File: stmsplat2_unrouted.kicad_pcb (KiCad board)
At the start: 2 copper layers, 100 x 100 mm, 113 parts, among them J1 C11_2X36, J10 Conn_01x03_Male, J11 Conn_01x02_Male, J12 Conn_01x04_Male, J13 Conn_01x04_Male, J14 Conn_01x02, J15 Conn_01x02, J16 Screw_Terminal_01x03, J17 Screw_Terminal_01x02, J2 C12_2X36, J3 Conn_01x04_Male, J4 Conn_01x04_Male, J5 Conn_Coaxial, J6 Conn_01x04_Male, J7 Conn_01x04_Male, J8 Conn_01x04_Male, J9 Conn_01x03_Male, Q1 BSS138LT1G, U1 ublox_chinese_PCB_module, U10 XCVR_E30-400M20S (Si4463), U11 3115_module, U2 ESP-C3-13U, U3 SST25VF032B, U4 48L512-48LM01, U5 Opamp_Quad_MCP6024, U6 E180-ZG120A, U7 AZ1084C, U8 MCP6S93-X_UN, U9 DS2485

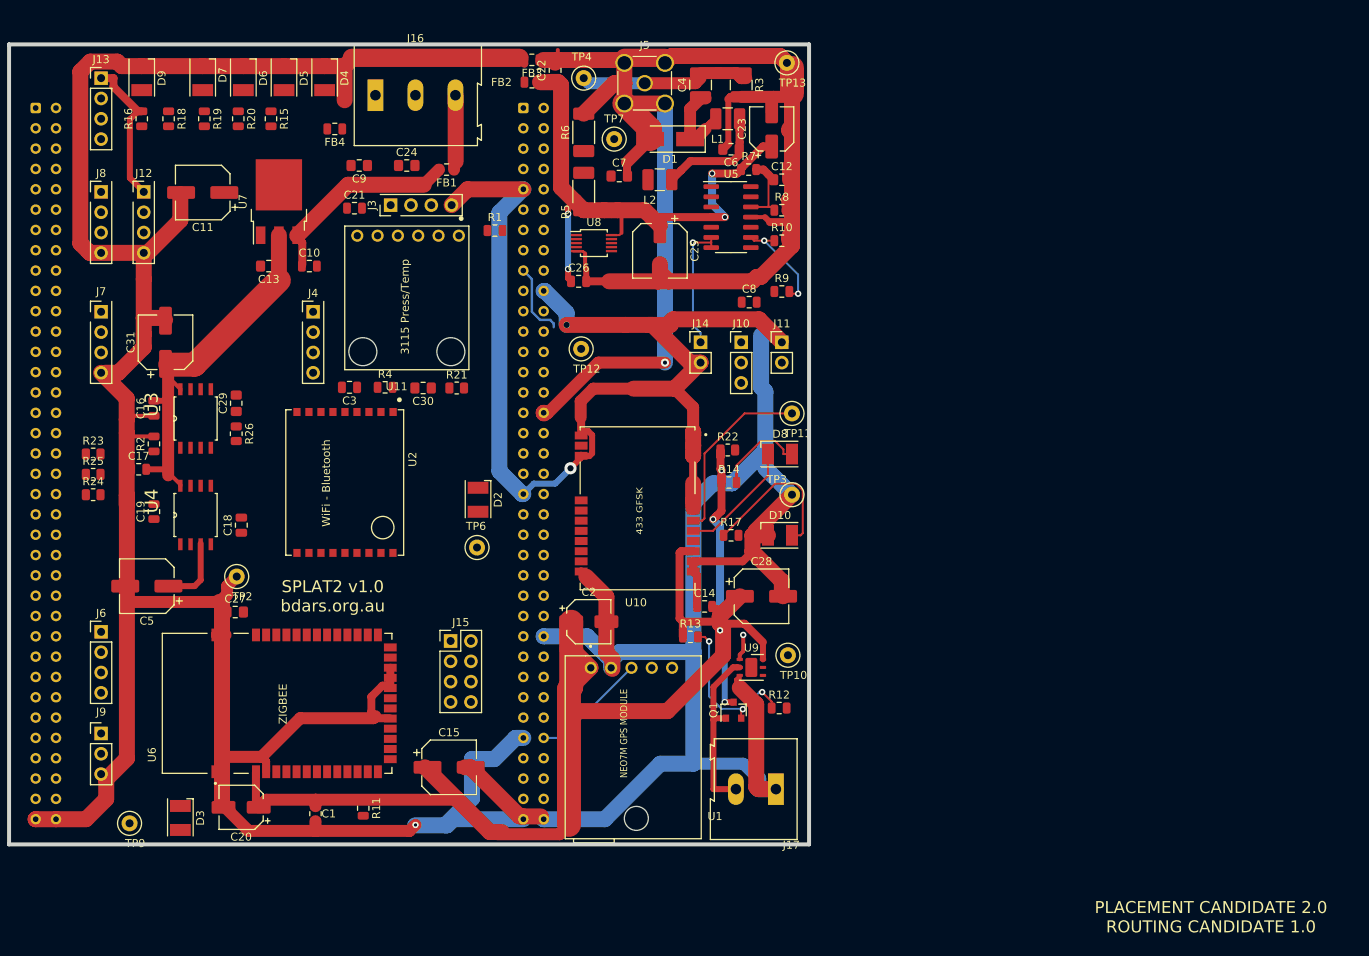
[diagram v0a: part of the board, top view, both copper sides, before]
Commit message: better placement, more handrouting, re-done power area etc
A few more passive comps added including dil switch
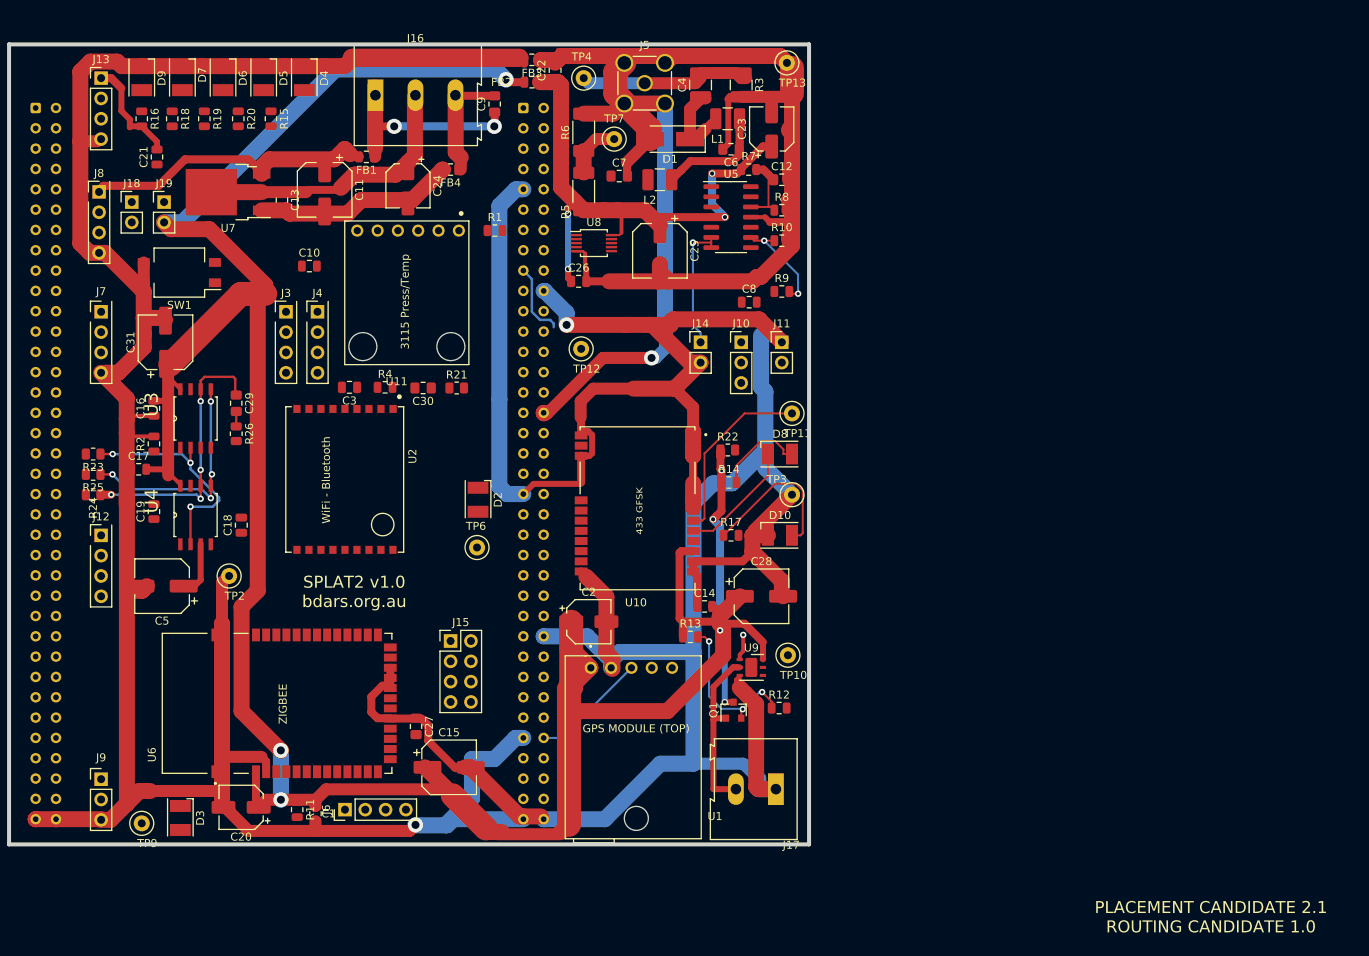
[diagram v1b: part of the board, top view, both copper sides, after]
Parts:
- added J18: Conn_01x02_Male, Connector_PinHeader_2.54mm:PinHeader_1x02_P2.54mm_Vertical, F.Cu at (67.3, 85.3)
- added J19: Conn_01x02_Male, Connector_PinHeader_2.54mm:PinHeader_1x02_P2.54mm_Vertical, F.Cu at (71.4, 85.3)
- added SW1: SW_DIP_x02, Button_Switch_SMD:SW_DIP_SPSTx02_Slide_Omron_A6S-210x_W8.9mm_P2.54mm, F.Cu at (73.3, 94.2)
- C24: value 0.1uF -> 10uF; footprint Capacitor_SMD:C_0805_2012Metric_Pad1.15x1.40mm_HandSolder -> Capacitor_SMD:CP_Elec_5x5.4
- moved J12 43.3 mm to (63.5, 127.0)
- moved J6 37.7 mm to (94.0, 161.3), turned to 90 degrees
- moved C27 26.7 mm to (102.9, 150.9), turned to 270 degrees
- moved C21 25.5 mm to (70.5, 79.7), turned to 90 degrees
- moved J3 18.7 mm to (86.6, 99.1), turned to 0 degrees
- moved C9 18.6 mm to (112.7, 73.1), turned to 90 degrees
- moved FB4 15.3 mm to (107.2, 81.3)
- moved C11 15.2 mm to (91.4, 83.8), turned to 270 degrees
- moved FB1 10.1 mm to (96.7, 79.7)
- moved C13 8.42 mm to (86.1, 85.1), turned to 270 degrees
- moved R11 8.26 mm to (88.0, 161.3)
- moved U7 6.46 mm to (79.4, 84.1), turned to 180 degrees
- moved J9 5.72 mm to (63.5, 157.5)
- moved C24 2.54 mm to (101.9, 83.3), turned to 270 degrees
- moved D5 2.54 mm to (83.8, 69.8)
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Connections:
- C13 pad 1: VDD -> Net-(C13-Pad1)
- C24 pad 1: VDD -> Net-(C13-Pad1)
- C24 pad 2: /RAWGND -> GND
- J1 pad 14: /NRST -> NRST
- J1 pad 4: /PD2 -> PD2
- J1 pad 45: /PD7 -> PD7
- J16 pad 1: /RAWGND -> /RAW5V
- J16 pad 2: VDD -> Net-(C13-Pad1)
- J16 pad 3: /RAW5V -> /RAWGND
- U7 pad 2: VDD -> Net-(C13-Pad1)
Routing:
- net VDD: track 248.0 -> 371.4 mm, vias 4 -> 7
- net /SPI2_SCKT: track 0.00 -> 35.1 mm, vias 0 -> 4
- net Net-(C13-Pad1): track 0.00 -> 34.6 mm
- net /SPI2_MOSIT: track 0.00 -> 28.9 mm, vias 0 -> 4
- net /SPI2_MISOT: track 0.00 -> 28.4 mm, vias 0 -> 3
- net /RAW5V: track 9.36 -> 25.3 mm, vias 0 -> 2
- net /RAWGND: track 0.00 -> 14.3 mm
- net +5V: track 25.1 -> 37.8 mm
- net GND: track 684.5 -> 694.1 mm, vias 3 -> 2
- net Net-(C7-Pad1): track 0.00 -> 7.09 mm
- net Net-(C5-Pad1): track 8.92 -> 6.92 mm
- net Net-(C29-Pad2): track 0.00 -> 1.85 mm
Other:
- board text added: "PLACEMENT CANDIDATE 2.1 ROUTING CANDIDATE 1.0"
- board text removed: "PLACEMENT CANDIDATE 2.0 ROUTING CANDIDATE 1.0"

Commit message: Splat2 Revision A.  Work-in-progress
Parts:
- removed REF**: ST_Morpho_Connector_144_STLink_MountingHoles, Module:ST_Morpho_Connector_144_STLink_MountingHoles
- D10, D2, D3, D4, D5, D6, D7, D8, D9: footprint LED_SMD:LED_PLCC-2 -> splat2footprints:LED_PLCC-2
- J1, J2: footprint Connector_Samtec_HLE_THT:Samtec_HLE-136-02-xx-DV-TE_2x36_P2.54mm_Horizontal -> Connector_PinSocket_2.54mm:PinSocket_2x36_P2.54mm_Vertical
- R5, R6: footprint Resistor_SMD:R_2010_5025Metric_Pad1.52x2.65mm_HandSolder -> Resistor_SMD:R_0805_2012Metric
- R7, R8: value 4K7 -> 1K
- moved R1 2.90 mm to (111.9, 86.1)
- moved TP10 2.07 mm to (149.8, 140.0)
- moved C2 0.93 mm to (125.3, 138.2)
- moved C11 0.51 mm to (90.9, 83.8)
- turned J1 to 180 degrees
- turned J2 to 180 degrees
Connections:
- net Net-(C13-Pad1) renamed /OUR3V3
- C1 pad 1: VDD -> +3V3
- C11 pad 1: +5V -> 5VEXT
- C14 pad 2: VDD -> +3V3
- C15 pad 1: VDD -> +3V3
- C16 pad 2: VDD -> +3V3
- C17 pad 2: VDD -> +3V3
- C18 pad 1: VDD -> +3V3
- C19 pad 2: VDD -> +3V3
- C2 pad 1: VDD -> +3V3
- C20 pad 1: VDD -> +3V3
- C21 pad 2: VDD -> +3V3
- C28 pad 1: VDD -> +3V3
- C3 pad 1: VDD -> +3V3
- C30 pad 1: VDD -> +3V3
- C31 pad 1: VDD -> +3V3
- FB1 pad 2: +5V -> 5VEXT
- FB2 pad 1: VDD -> +3V3
- J1 pad 16: /+3V3 -> +3V3
- J1 pad 38: /PC0 -> GND
- J1 pad 5: VDD -> /3V3_VPP
- J1 pad 57: /PD0 -> PD0
- J1 pad 6: +5V -> 5VEXT
- J12 pad 1: VDD -> +3V3
- J13 pad 1: VDD -> +3V3
- J19 pad 2: VDD -> +3V3
- J4 pad 1: VDD -> +3V3
- J7 pad 1: VDD -> +3V3
- Q1 pad 3: VDD -> +3V3
- R1 pad 1: VDD -> +3V3
- R10 pad 2: GNDA -> /HALF3V3
- R11 pad 1: VDD -> +3V3
- R13 pad 1: VDD -> +3V3
- R14 pad 1: VDD -> +3V3
- R16 pad 2: VDD -> +3V3
- R21 pad 1: VDD -> +3V3
- R22 pad 1: VDD -> +3V3
- R4 pad 1: VDD -> +3V3
- U1 pad 1: VDD -> +3V3
- U10 pad 9: VDD -> +3V3
- U11 pad 1: PB9 -> PD0
- U11 pad 5: VDD -> +3V3
- U2 pad 1: VDD -> +3V3
- U3 pad 8: VDD -> +3V3
- U4 pad 8: VDD -> +3V3
- U6 pad 3: VDD -> +3V3
- U7 pad 3: +5V -> 5VEXT
- U9 pad 6: VDD -> +3V3
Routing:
- net +3V3: track 0.00 -> 573.0 mm, vias 0 -> 8
- net VDD: track 371.4 -> 0.00 mm, vias 7 -> 0
- net GND: track 694.1 -> 905.4 mm, vias 2 -> 3
- net PC11: track 0.00 -> 136.0 mm, vias 0 -> 4
- net /HALF3V3: track 0.00 -> 56.7 mm, vias 0 -> 2
- net Net-(J12-Pad2): track 0.00 -> 46.9 mm, vias 0 -> 2
- net Net-(TP9-Pad1): track 0.00 -> 46.5 mm, vias 0 -> 1
- net 5VEXT: track 0.00 -> 45.7 mm, vias 0 -> 1
- net Net-(D2-Pad1): track 0.00 -> 45.3 mm, vias 0 -> 2
- net Net-(D3-Pad1): track 0.00 -> 41.7 mm, vias 0 -> 2
- net PA3: track 0.00 -> 39.5 mm, vias 0 -> 1
- net Net-(C7-Pad1): track 7.09 -> 45.3 mm, vias 0 -> 2
- net PG4: track 0.00 -> 35.3 mm, vias 0 -> 2
- net Net-(J12-Pad3): track 0.00 -> 33.2 mm, vias 0 -> 1
- net PD2: track 0.00 -> 32.6 mm, vias 0 -> 1
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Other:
- rule pad_to_mask_clearance: 0.2 -> 0
- board text added: "1"
- board text added: "1W"
- board text added: "3V3"
- board text added: "5VIN"
- board text added: "COM2"
- board text added: "COM7"
- board text added: "I2C2"
- board text added: "INT3V"
- board text added: "J-LNK"
- board text added: "J1"
- board text added: "J14: DAC O/P J10: SELECT J11: SPEAKER"
- board text added: "J2"
- board text added: "RST"
- board text added: "SPLAT2 DEVELOPMENT BOARD Rev A"
- board text added: "SPLAT2 RevA bdars.org.au"
- board text removed: "AGND"
- board text removed: "PLACEMENT CANDIDATE 2.1 ROUTING CANDIDATE 1.0"
- board text removed: "SER"
- board text removed: "SPLAT2 v1.0 bdars.org.au"

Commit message: Routed but needs checking
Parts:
- added J20: Conn_01x02_Male, Connector_PinHeader_2.54mm:PinHeader_1x02_P2.54mm_Vertical, F.Cu at (85.8, 91.7)
- D10, D3, D4, D5, D6, D7, D8, D9: footprint splat2footprints:LED_PLCC-2 -> splat2-kicad:LED_PLCC-2
- D2: footprint splat2footprints:LED_PLCC-2 -> LED_SMD:LED_PLCC-2
- J9: value Conn_01x03_Male -> Conn_01x04_Male; footprint Connector_PinHeader_2.54mm:PinHeader_1x03_P2.54mm_Vertical -> Connector_PinHeader_2.54mm:PinHeader_1x04_P2.54mm_Vertical
- U2: footprint ESP-C3-13 -> splat2-kicad:ESP-C3-13
- moved J9 17.7 mm to (63.6, 139.8)
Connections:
- net /PF6 renamed PF6
- J1 pad 18: +5V -> +5VSTM
- J2 pad 18: /PB11 -> PB11
- J9 pad 1: PF1 -> +3V3
- J9 pad 2: PF0 -> PF1
- J9 pad 3: GND -> PF0
- U6 pad 17: Net-(U6-Pad17) -> PB11
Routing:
- net PC11: track 136.0 -> 0.00 mm, vias 4 -> 0
- net +5V: track 6.52 -> 56.7 mm, vias 0 -> 1
- net Net-(J12-Pad2): track 46.9 -> 0.00 mm, vias 2 -> 0
- net Net-(D2-Pad1): track 45.3 -> 0.00 mm, vias 2 -> 0
- net PG4: track 35.3 -> 0.00 mm, vias 2 -> 0
- net PD2: track 32.6 -> 0.00 mm, vias 1 -> 0
- net Net-(J3-Pad2): track 30.8 -> 0.00 mm, vias 1 -> 0
- net Net-(J3-Pad3): track 28.8 -> 0.00 mm, vias 1 -> 0
- net Net-(J4-Pad3): track 27.0 -> 0.00 mm, vias 1 -> 0
- net Net-(D2-Pad2): track 23.8 -> 0.00 mm
- net PB6: track 20.7 -> 0.00 mm
- net Net-(J4-Pad2): track 14.1 -> 0.00 mm, vias 1 -> 0
- net NRST: track 14.0 -> 0.00 mm
- net 5VEXT: track 45.7 -> 58.0 mm, vias 1 -> 2
- net Net-(D8-Pad2): track 11.9 -> 0.00 mm
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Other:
- board text added: "INT5V"
